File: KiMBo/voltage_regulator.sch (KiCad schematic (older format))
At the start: 6 parts, among them U3 LM2592HVSX-5.0

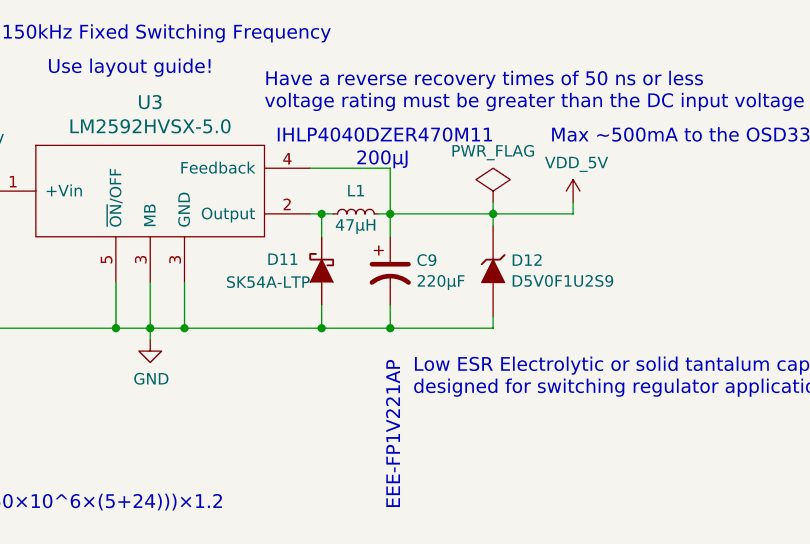
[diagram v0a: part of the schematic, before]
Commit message: More footprint association
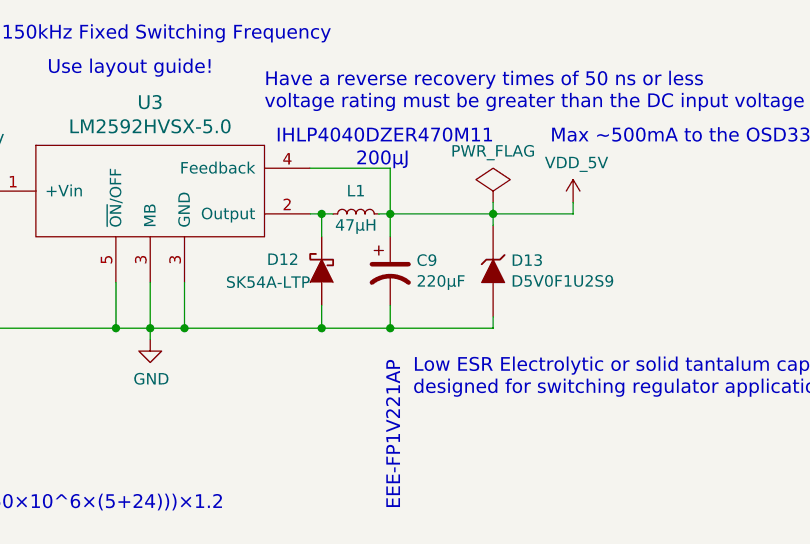
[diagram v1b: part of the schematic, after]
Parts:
- D12: renamed from D11; footprint (none) -> KiMBo:SK-DO-214AC
- D13: renamed from D12; footprint (none) -> KiMBo:SOD-923
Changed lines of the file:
@@
 $EndDescr
 $Comp
-L PWR_FLAG #FLG074
+L PWR_FLAG #FLG075
 U 1 1 578901B0
 P 9200 4950
-F 0 "#FLG074" H 9200 5045 50  0001 C CNN
+F 0 "#FLG075" H 9200 5045 50  0001 C CNN
 F 1 "PWR_FLAG" H 9200 5174 50  0000 C CNN
 F 2 "" H 9200 4950 50  0000 C CNN
@@
 $EndComp
 $Comp
-L VDD_5V #PWR075
+L VDD_5V #PWR076
 U 1 1 59E9FFBE
 P 9550 4950
-F 0 "#PWR075" H 9550 4800 50  0001 C CNN
+F 0 "#PWR076" H 9550 4800 50  0001 C CNN
 F 1 "VDD_5V" H 9565 5123 50  0000 C CNN
 F 2 "" H 9550 4950 50  0000 C CNN
@@
 $EndComp
 $Comp
-L +24V #PWR076
+L +24V #PWR077
 U 1 1 59F3325A
 P 6950 4850
-F 0 "#PWR076" H 6950 4700 50  0001 C CNN
+F 0 "#PWR077" H 6950 4700 50  0001 C CNN
 F 1 "+24V" H 6965 5023 50  0000 C CNN
 F 2 "" H 6950 4850 50  0000 C CNN
@@
 Use layout guide!
 $Comp
-L ZENER D12
+L ZENER D13
 U 1 1 5B7841ED
 P 9200 5250
-F 0 "D12" V 9154 5329 50  0000 L CNN
+F 0 "D13" V 9154 5329 50  0000 L CNN
 F 1 "D5V0F1U2S9" V 9245 5329 50  0000 L CNN
-F 2 "" H 9200 5250 50  0001 C CNN
+F 2 "KiMBo:SOD-923" H 9200 5250 50  0001 C CNN
 F 3 "" H 9200 5250 50  0000 C CNN
 	1    9200 5250
@@
 $EndComp
 $Comp
-L D_Schottky D11
+L D_Schottky D12
 U 1 1 5B78FD55
 P 8450 5250
-F 0 "D11" V 8400 5350 50  0000 L CNN
+F 0 "D12" V 8400 5350 50  0000 L CNN
 F 1 "SK54A-LTP" V 8500 5300 50  0000 L CNN
-F 2 "" H 8450 5250 50  0001 C CNN
+F 2 "KiMBo:SK-DO-214AC" H 8450 5250 50  0001 C CNN
 F 3 "" H 8450 5250 50  0000 C CNN
 	1    8450 5250
@@
 Connection ~ 6950 4900
 $Comp
-L GND #PWR077
+L GND #PWR078
 U 1 1 59010253
 P 7700 5550
-F 0 "#PWR077" H 7700 5300 50  0001 C CNN
+F 0 "#PWR078" H 7700 5300 50  0001 C CNN
 F 1 "GND" H 7705 5377 50  0000 C CNN
 F 2 "" H 7700 5550 50  0000 C CNN

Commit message: Create more footprints and add more associations
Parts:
- L1: footprint (none) -> KiMBo:IHLP_Inductor
- U3: footprint (none) -> TO_SOT_Packages_SMD:TO-263-5Lead
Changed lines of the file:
@@
 F 0 "L1" V 8700 5000 50  0000 C CNN
 F 1 "47μH" V 8550 5000 50  0000 C CNN
-F 2 "" H 8600 5000 50  0001 C CNN
+F 2 "KiMBo:IHLP_Inductor" H 8600 5000 50  0001 C CNN
 F 3 "" H 8600 5000 50  0000 C CNN
 	1    8600 5000
@@
 F 0 "U3" H 7700 5287 60  0000 C CNN
 F 1 "LM2592HVSX-5.0" H 7700 5181 60  0000 C CNN
-F 2 "" H 7550 4900 60  0001 C CNN
+F 2 "TO_SOT_Packages_SMD:TO-263-5Lead" H 7550 4900 60  0001 C CNN
 F 3 "" H 7550 4900 60  0001 C CNN
 	1    7700 4900

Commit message: Add more footprints and more associations, one association left!
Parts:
- C8: footprint (none) -> KiMBo:c_elec_16x16.5
- C9: footprint (none) -> KiMBo:c_elec_8x10.2
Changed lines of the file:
@@
 F 0 "C8" H 7065 5296 50  0000 L CNN
 F 1 "470μF" H 7065 5205 50  0000 L CNN
-F 2 "" H 6950 5250 50  0001 C CNN
+F 2 "KiMBo:c_elec_16x16.5" H 6950 5250 50  0001 C CNN
 F 3 "" H 6950 5250 50  0000 C CNN
 	1    6950 5250
@@
 F 0 "C9" H 8865 5296 50  0000 L CNN
 F 1 "220μF" H 8865 5205 50  0000 L CNN
-F 2 "" H 8750 5250 50  0001 C CNN
+F 2 "KiMBo:c_elec_8x10.2" H 8750 5250 50  0001 C CNN
 F 3 "" H 8750 5250 50  0000 C CNN
 	1    8750 5250

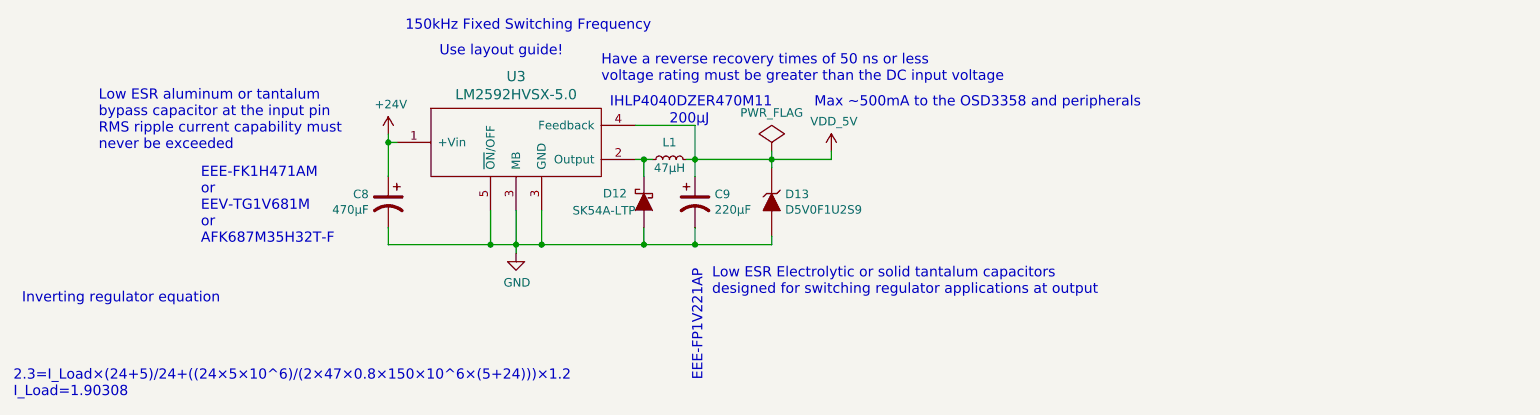
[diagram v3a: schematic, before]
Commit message: Begin layout
Arrange all connectors to get a feel for the area.
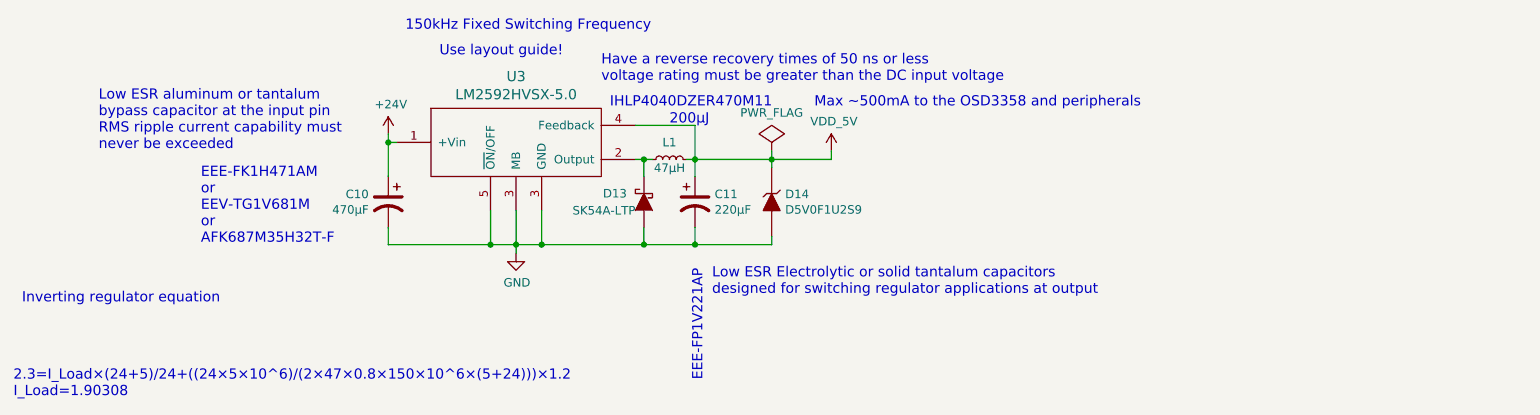
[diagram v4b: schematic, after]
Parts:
- renumbered C8 to C10, C9 to C11, D12 to D13, D13 to D14
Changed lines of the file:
@@
 $EndDescr
 $Comp
-L PWR_FLAG #FLG075
+L PWR_FLAG #FLG078
 U 1 1 578901B0
 P 9200 4950
-F 0 "#FLG075" H 9200 5045 50  0001 C CNN
+F 0 "#FLG078" H 9200 5045 50  0001 C CNN
 F 1 "PWR_FLAG" H 9200 5174 50  0000 C CNN
 F 2 "" H 9200 4950 50  0000 C CNN
@@
 $EndComp
 $Comp
-L VDD_5V #PWR076
+L VDD_5V #PWR079
 U 1 1 59E9FFBE
 P 9550 4950
-F 0 "#PWR076" H 9550 4800 50  0001 C CNN
+F 0 "#PWR079" H 9550 4800 50  0001 C CNN
 F 1 "VDD_5V" H 9565 5123 50  0000 C CNN
 F 2 "" H 9550 4950 50  0000 C CNN
@@
 $EndComp
 $Comp
-L +24V #PWR077
+L +24V #PWR080
 U 1 1 59F3325A
 P 6950 4850
-F 0 "#PWR077" H 6950 4700 50  0001 C CNN
+F 0 "#PWR080" H 6950 4700 50  0001 C CNN
 F 1 "+24V" H 6965 5023 50  0000 C CNN
 F 2 "" H 6950 4850 50  0000 C CNN
@@
 Use layout guide!
 $Comp
-L ZENER D13
+L ZENER D14
 U 1 1 5B7841ED
 P 9200 5250
-F 0 "D13" V 9154 5329 50  0000 L CNN
+F 0 "D14" V 9154 5329 50  0000 L CNN
 F 1 "D5V0F1U2S9" V 9245 5329 50  0000 L CNN
 F 2 "KiMBo:SOD-923" H 9200 5250 50  0001 C CNN
@@
 $EndComp
 $Comp
-L D_Schottky D12
+L D_Schottky D13
 U 1 1 5B78FD55
 P 8450 5250
-F 0 "D12" V 8400 5350 50  0000 L CNN
+F 0 "D13" V 8400 5350 50  0000 L CNN
 F 1 "SK54A-LTP" V 8500 5300 50  0000 L CNN
 F 2 "KiMBo:SK-DO-214AC" H 8450 5250 50  0001 C CNN
@@
 Connection ~ 6950 4900
 $Comp
-L GND #PWR078
+L GND #PWR081
 U 1 1 59010253
 P 7700 5550
-F 0 "#PWR078" H 7700 5300 50  0001 C CNN
+F 0 "#PWR081" H 7700 5300 50  0001 C CNN
 F 1 "GND" H 7705 5377 50  0000 C CNN
 F 2 "" H 7700 5550 50  0000 C CNN
@@
 Inverting regulator equation
 $Comp
-L CP1 C8
+L CP1 C10
 U 1 1 591FE1CF
 P 6950 5250
-F 0 "C8" H 7065 5296 50  0000 L CNN
+F 0 "C10" H 7065 5296 50  0000 L CNN
 F 1 "470μF" H 7065 5205 50  0000 L CNN
 F 2 "KiMBo:c_elec_16x16.5" H 6950 5250 50  0001 C CNN
@@
 $EndComp
 $Comp
-L CP1 C9
+L CP1 C11
 U 1 1 591FE334
 P 8750 5250
-F 0 "C9" H 8865 5296 50  0000 L CNN
+F 0 "C11" H 8865 5296 50  0000 L CNN
 F 1 "220μF" H 8865 5205 50  0000 L CNN
 F 2 "KiMBo:c_elec_8x10.2" H 8750 5250 50  0001 C CNN

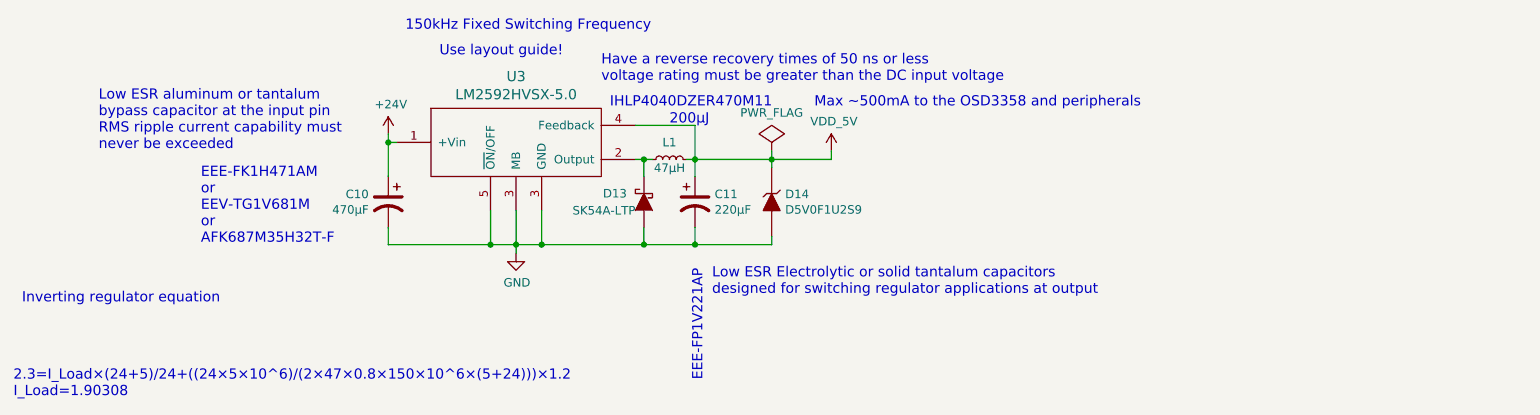
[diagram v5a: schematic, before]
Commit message: Add F1 PTC resettable fuse at the 5V output, begin E's heater circuit layout
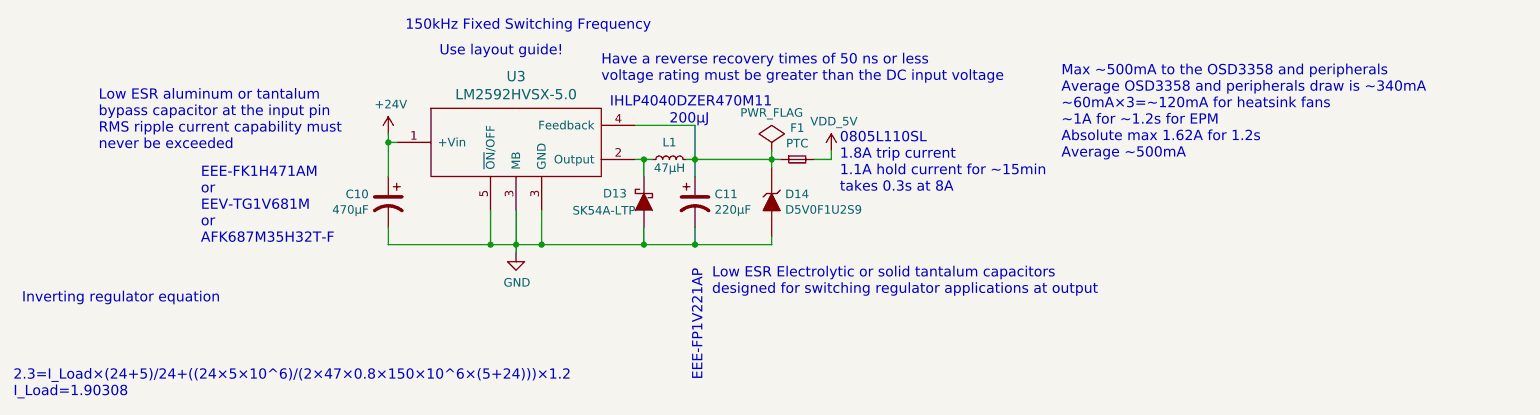
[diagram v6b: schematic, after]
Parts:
- added F1: PTC, symbol FUSE_Small
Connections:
- net VDD_5V: now also F1.2; no longer C11.1, D14.1 (K), L1.2, U3.4 (Feedback)
- new net: C11.1, D14.1 (K), F1.1, L1.2, U3.4 (Feedback)
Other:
- note added: "0805L110SL\n1.8A trip current\n1.1A hold current for ~~15min\ntakes 0.3s at 8A"
- note added: "Max ~~500mA to the OSD3358 and peripherals\nAverage OSD3358 and peripherals draw is ~~340mA\n~~60mA×3=~~120mA for heatsink fans\n~~1A for ~~1.2s for EPM\nAbsolute max 1.62A for 1.2s\nAverage ~~500mA"
- note removed: "Max ~~500mA to the OSD3358 and peripherals"
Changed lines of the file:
@@
 Text Notes 5850 5500 0    60   ~ 0
 EEE-FK1H471AM\nor\nEEV-TG1V681M\nor\nAFK687M35H32T-F
-Text Notes 9450 4700 0    60   ~ 0
-Max ~~500mA to the OSD3358 and peripherals
+Text Notes 10900 5000 0    60   ~ 0
+Max ~~500mA to the OSD3358 and peripherals\nAverage OSD3358 and peripherals draw is ~~340mA\n~~60mA×3=~~120mA for heatsink fans\n~~1A for ~~1.2s for EPM\nAbsolute max 1.62A for 1.2s\nAverage ~~500mA
 Text Notes 4750 6400 0    60   ~ 0
 2.3=I_Load×(24+5)/24+((24×5×10^6)/(2×47×0.8×150×10^6×(5+24)))×1.2\nI_Load=1.90308
@@
 	7550 5300 7550 5500
 Wire Wire Line
-	6950 5500 9200 5500
+	6950 5500 7550 5500
+Wire Wire Line
+	7550 5500 7700 5500
+Wire Wire Line
+	7700 5500 7850 5500
+Wire Wire Line
+	7850 5500 8450 5500
+Wire Wire Line
+	8450 5500 8750 5500
+Wire Wire Line
+	8750 5500 9200 5500
 Wire Wire Line
 	7850 5500 7850 5300
 Wire Wire Line
-	7700 5300 7700 5550
+	7700 5300 7700 5500
+Wire Wire Line
+	7700 5500 7700 5550
 Connection ~ 7700 5500
 Wire Wire Line
@@
 	8450 5100 8450 5000
 Wire Wire Line
-	8400 5000 8500 5000
+	8400 5000 8450 5000
+Wire Wire Line
+	8450 5000 8500 5000
 Connection ~ 8450 5000
 Text Notes 7050 4250 0    60   ~ 0
 150kHz Fixed Switching Frequency
 Wire Wire Line
-	8750 4800 8750 5100
-Wire Wire Line
-	8700 5000 9550 5000
+	8750 4800 8750 5000
+Wire Wire Line
+	8750 5000 8750 5100
+Wire Wire Line
+	8700 5000 8750 5000
+Wire Wire Line
+	8750 5000 9200 5000
+Wire Wire Line
+	9200 5000 9250 5000
 Wire Wire Line
 	8750 5500 8750 5400
 Connection ~ 8450 5500
 Wire Wire Line
-	6950 4850 6950 5100
+	6950 4850 6950 4900
+Wire Wire Line
+	6950 4900 6950 5100
 Wire Wire Line
 	6950 4900 7000 4900
@@
 Connection ~ 7550 5500
 Wire Wire Line
-	9200 4950 9200 5050
+	9200 4950 9200 5000
+Wire Wire Line
+	9200 5000 9200 5050
 Connection ~ 8750 5000
 Wire Wire Line
@@
 	1    0    0    -1
 $EndComp
+$Comp
+L FUSE_Small F1
+U 1 1 591C13CD
+P 9350 5000
+F 0 "F1" H 9350 5185 50  0000 C CNN
+F 1 "PTC" H 9350 5094 50  0000 C CNN
+F 2 "" H 9350 5000 50  0000 C CNN
+F 3 "" H 9350 5000 50  0000 C CNN
+	1    9350 5000
+	1    0    0    -1
+$EndComp
+Wire Wire Line
+	9450 5000 9550 5000
+Text Notes 9600 5200 0    60   ~ 0
+0805L110SL\n1.8A trip current\n1.1A hold current for ~~15min\ntakes 0.3s at 8A
 $EndSCHEMATC

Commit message: Daisy chain the SPI stepper motor driver interface, continue work on the E-heater layout
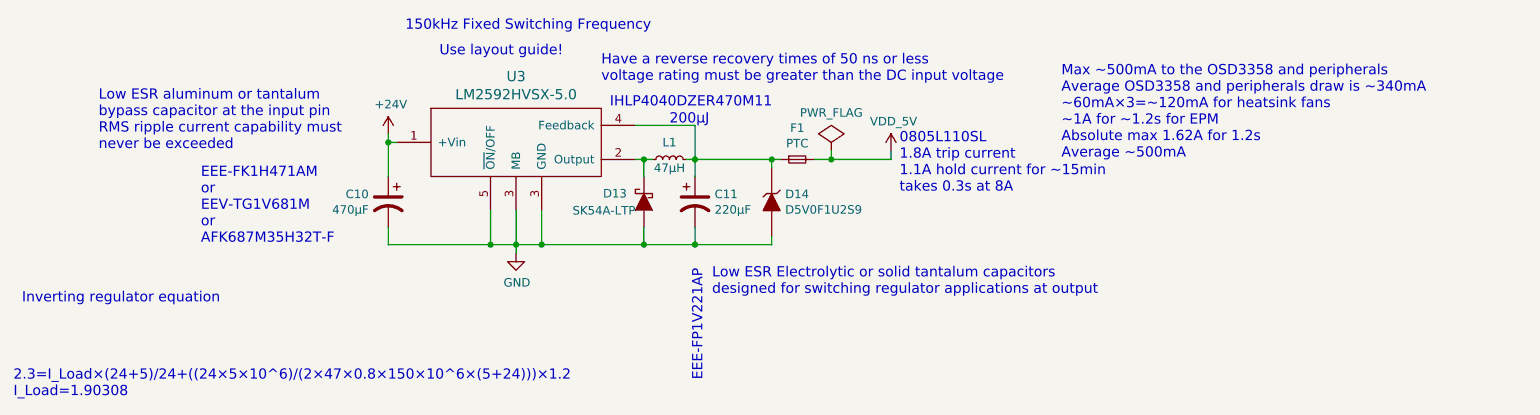
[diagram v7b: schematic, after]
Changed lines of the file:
@@
 $EndDescr
 $Comp
-L PWR_FLAG #FLG076
+L PWR_FLAG #FLG13
 U 1 1 578901B0
-P 9200 4950
-F 0 "#FLG076" H 9200 5045 50  0001 C CNN
-F 1 "PWR_FLAG" H 9200 5174 50  0000 C CNN
-F 2 "" H 9200 4950 50  0000 C CNN
-F 3 "" H 9200 4950 50  0000 C CNN
-	1    9200 4950
-	1    0    0    -1
-$EndComp
-$Comp
-L VDD_5V #PWR077
-U 1 1 59E9FFBE
 P 9550 4950
-F 0 "#PWR077" H 9550 4800 50  0001 C CNN
-F 1 "VDD_5V" H 9565 5123 50  0000 C CNN
+F 0 "#FLG13" H 9550 5045 50  0001 C CNN
+F 1 "PWR_FLAG" H 9550 5174 50  0000 C CNN
 F 2 "" H 9550 4950 50  0000 C CNN
 F 3 "" H 9550 4950 50  0000 C CNN
@@
 $EndComp
 $Comp
-L +24V #PWR078
+L VDD_5V #PWR66
+U 1 1 59E9FFBE
+P 9900 4950
+F 0 "#PWR66" H 9900 4800 50  0001 C CNN
+F 1 "VDD_5V" H 9915 5123 50  0000 C CNN
+F 2 "" H 9900 4950 50  0000 C CNN
+F 3 "" H 9900 4950 50  0000 C CNN
+	1    9900 4950
+	1    0    0    -1
+$EndComp
+$Comp
+L +24V #PWR64
 U 1 1 59F3325A
 P 6950 4850
-F 0 "#PWR078" H 6950 4700 50  0001 C CNN
+F 0 "#PWR64" H 6950 4700 50  0001 C CNN
 F 1 "+24V" H 6965 5023 50  0000 C CNN
 F 2 "" H 6950 4850 50  0000 C CNN
@@
 	7550 5300 7550 5500
 Wire Wire Line
-	6950 5500 7550 5500
-Wire Wire Line
-	7550 5500 7700 5500
-Wire Wire Line
-	7700 5500 7850 5500
-Wire Wire Line
-	7850 5500 8450 5500
-Wire Wire Line
-	8450 5500 8750 5500
-Wire Wire Line
-	8750 5500 9200 5500
+	6950 5500 9200 5500
 Wire Wire Line
 	7850 5500 7850 5300
 Wire Wire Line
-	7700 5300 7700 5500
-Wire Wire Line
-	7700 5500 7700 5550
+	7700 5300 7700 5550
 Connection ~ 7700 5500
 Wire Wire Line
@@
 	8450 5100 8450 5000
 Wire Wire Line
-	8400 5000 8450 5000
-Wire Wire Line
-	8450 5000 8500 5000
+	8400 5000 8500 5000
 Connection ~ 8450 5000
 Text Notes 7050 4250 0    60   ~ 0
 150kHz Fixed Switching Frequency
 Wire Wire Line
-	8750 4800 8750 5000
-Wire Wire Line
-	8750 5000 8750 5100
-Wire Wire Line
-	8700 5000 8750 5000
-Wire Wire Line
-	8750 5000 9200 5000
-Wire Wire Line
-	9200 5000 9250 5000
+	8750 4800 8750 5100
+Wire Wire Line
+	8700 5000 9250 5000
 Wire Wire Line
 	8750 5500 8750 5400
 Connection ~ 8450 5500
 Wire Wire Line
-	6950 4850 6950 4900
-Wire Wire Line
-	6950 4900 6950 5100
+	6950 4850 6950 5100
 Wire Wire Line
 	6950 4900 7000 4900
@@
 	6950 5400 6950 5500
 Connection ~ 7550 5500
-Wire Wire Line
-	9200 4950 9200 5000
 Wire Wire Line
 	9200 5000 9200 5050
@@
 	8400 4800 8750 4800
 Wire Wire Line
-	9550 5000 9550 4950
+	9900 5000 9900 4950
 Connection ~ 6950 4900
 $Comp
-L GND #PWR079
+L GND #PWR65
 U 1 1 59010253
 P 7700 5550
-F 0 "#PWR079" H 7700 5300 50  0001 C CNN
+F 0 "#PWR65" H 7700 5300 50  0001 C CNN
 F 1 "GND" H 7705 5377 50  0000 C CNN
 F 2 "" H 7700 5550 50  0000 C CNN
@@
 $EndComp
 Wire Wire Line
-	9450 5000 9550 5000
-Text Notes 9600 5200 0    60   ~ 0
+	9450 5000 9900 5000
+Text Notes 9950 5200 0    60   ~ 0
 0805L110SL\n1.8A trip current\n1.1A hold current for ~~15min\ntakes 0.3s at 8A
+Wire Wire Line
+	9550 4950 9550 5000
+Connection ~ 9550 5000
 $EndSCHEMATC
